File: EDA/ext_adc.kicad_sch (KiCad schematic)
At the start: 10 parts, among them U1 ADS1115IDGS, U2 ADS1115IDGS

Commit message: Renumber schematic
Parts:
- renumbered C4 to C13, C5 to C14, R1 to R42, R2 to R43, R3 to R44, R4 to R45, R5 to R46, R6 to R47, U1 to U7, U2 to U8
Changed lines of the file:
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@@
   (symbol (lib_id "Library:R") (at 114.3 124.46 0) (unit 1)
     (in_bom yes) (on_board yes) (dnp no)
-    (property "Reference" "R3" (at 113.03 119.38 90)
+    (property "Reference" "R44" (at 113.03 119.38 90)
       (effects (font (size 1.27 1.27)) hide)
     )
@@
       (project "DiveCAN Head2"
         (path "/ab021047-3849-453b-b3dc-d234ace3779d/43f35934-7d95-448c-989a-d83dd71666be"
-          (reference "R3") (unit 1)
+          (reference "R44") (unit 1)
         )
       )
@@
   (symbol (lib_id "Library:R") (at 114.3 132.08 0) (unit 1)
     (in_bom yes) (on_board yes) (dnp no)
-    (property "Reference" "R4" (at 113.03 127 90)
+    (property "Reference" "R45" (at 113.03 127 90)
       (effects (font (size 1.27 1.27)) hide)
     )
@@
       (project "DiveCAN Head2"
         (path "/ab021047-3849-453b-b3dc-d234ace3779d/43f35934-7d95-448c-989a-d83dd71666be"
-          (reference "R4") (unit 1)
+          (reference "R45") (unit 1)
         )
       )
@@
   (symbol (lib_id "Library:ADS1115IDGS") (at 133.35 128.27 0) (unit 1)
     (in_bom yes) (on_board yes) (dnp no) (fields_autoplaced)
-    (property "Reference" "U2" (at 135.5441 137.6101 0)
+    (property "Reference" "U8" (at 135.5441 137.6101 0)
       (effects (font (size 1.27 1.27)) (justify left))
     )
@@
       (project "DiveCAN Head2"
         (path "/ab021047-3849-453b-b3dc-d234ace3779d/43f35934-7d95-448c-989a-d83dd71666be"
-          (reference "U2") (unit 1)
+          (reference "U8") (unit 1)
         )
       )
@@
   (symbol (lib_id "Library:C") (at 139.7 55.88 0) (unit 1)
     (in_bom yes) (on_board yes) (dnp no) (fields_autoplaced)
-    (property "Reference" "C4" (at 142.621 54.856 0)
+    (property "Reference" "C13" (at 142.621 54.856 0)
       (effects (font (size 1.27 1.27)) (justify left))
     )
@@
       (project "DiveCAN Head2"
         (path "/ab021047-3849-453b-b3dc-d234ace3779d/43f35934-7d95-448c-989a-d83dd71666be"
-          (reference "C4") (unit 1)
+          (reference "C13") (unit 1)
         )
       )
@@
   (symbol (lib_id "power:GNDREF") (at 119.38 92.71 0) (unit 1)
     (in_bom yes) (on_board yes) (dnp no) (fields_autoplaced)
-    (property "Reference" "#PWR07" (at 119.38 99.06 0)
+    (property "Reference" "#PWR054" (at 119.38 99.06 0)
       (effects (font (size 1.27 1.27)) hide)
     )
@@
       (project "DiveCAN Head2"
         (path "/ab021047-3849-453b-b3dc-d234ace3779d/43f35934-7d95-448c-989a-d83dd71666be"
-          (reference "#PWR07") (unit 1)
+          (reference "#PWR054") (unit 1)
         )
       )
@@
   (symbol (lib_id "Library:R") (at 119.38 88.9 0) (unit 1)
     (in_bom yes) (on_board yes) (dnp no)
-    (property "Reference" "R6" (at 118.11 83.82 90)
+    (property "Reference" "R47" (at 118.11 83.82 90)
       (effects (font (size 1.27 1.27)) hide)
     )
@@
       (project "DiveCAN Head2"
         (path "/ab021047-3849-453b-b3dc-d234ace3779d/43f35934-7d95-448c-989a-d83dd71666be"
-          (reference "R6") (unit 1)
+          (reference "R47") (unit 1)
         )
       )
@@
   (symbol (lib_id "power:GNDREF") (at 109.22 82.55 0) (unit 1)
     (in_bom yes) (on_board yes) (dnp no) (fields_autoplaced)
-    (property "Reference" "#PWR03" (at 109.22 88.9 0)
+    (property "Reference" "#PWR052" (at 109.22 88.9 0)
       (effects (font (size 1.27 1.27)) hide)
     )
@@
       (project "DiveCAN Head2"
         (path "/ab021047-3849-453b-b3dc-d234ace3779d/43f35934-7d95-448c-989a-d83dd71666be"
-          (reference "#PWR03") (unit 1)
+          (reference "#PWR052") (unit 1)
         )
       )
@@
   (symbol (lib_id "power:GNDREF") (at 114.3 135.89 0) (unit 1)
     (in_bom yes) (on_board yes) (dnp no) (fields_autoplaced)
-    (property "Reference" "#PWR04" (at 114.3 142.24 0)
+    (property "Reference" "#PWR053" (at 114.3 142.24 0)
       (effects (font (size 1.27 1.27)) hide)
     )
@@
       (project "DiveCAN Head2"
         (path "/ab021047-3849-453b-b3dc-d234ace3779d/43f35934-7d95-448c-989a-d83dd71666be"
-          (reference "#PWR04") (unit 1)
+          (reference "#PWR053") (unit 1)
         )
       )
@@
   (symbol (lib_id "power:GNDREF") (at 133.35 138.43 0) (unit 1)
     (in_bom yes) (on_board yes) (dnp no) (fields_autoplaced)
-    (property "Reference" "#PWR012" (at 133.35 144.78 0)
+    (property "Reference" "#PWR056" (at 133.35 144.78 0)
       (effects (font (size 1.27 1.27)) hide)
     )
@@
       (project "DiveCAN Head2"
         (path "/ab021047-3849-453b-b3dc-d234ace3779d/43f35934-7d95-448c-989a-d83dd71666be"
-          (reference "#PWR012") (unit 1)
+          (reference "#PWR056") (unit 1)
         )
       )
@@
   (symbol (lib_id "Library:R") (at 109.22 71.12 0) (unit 1)
     (in_bom yes) (on_board yes) (dnp no)
-    (property "Reference" "R1" (at 107.95 66.04 90)
+    (property "Reference" "R42" (at 107.95 66.04 90)
       (effects (font (size 1.27 1.27)) hide)
     )
@@
       (project "DiveCAN Head2"
         (path "/ab021047-3849-453b-b3dc-d234ace3779d/43f35934-7d95-448c-989a-d83dd71666be"
-          (reference "R1") (unit 1)
+          (reference "R42") (unit 1)
         )
       )
@@
   (symbol (lib_id "Library:R") (at 119.38 81.28 0) (unit 1)
     (in_bom yes) (on_board yes) (dnp no)
-    (property "Reference" "R5" (at 118.11 76.2 90)
+    (property "Reference" "R46" (at 118.11 76.2 90)
       (effects (font (size 1.27 1.27)) hide)
     )
@@
       (project "DiveCAN Head2"
         (path "/ab021047-3849-453b-b3dc-d234ace3779d/43f35934-7d95-448c-989a-d83dd71666be"
-          (reference "R5") (unit 1)
+          (reference "R46") (unit 1)
         )
       )
@@
   (symbol (lib_id "power:GNDREF") (at 143.51 80.01 90) (unit 1)
     (in_bom yes) (on_board yes) (dnp no) (fields_autoplaced)
-    (property "Reference" "#PWR015" (at 149.86 80.01 0)
+    (property "Reference" "#PWR059" (at 149.86 80.01 0)
       (effects (font (size 1.27 1.27)) hide)
     )
@@
       (project "DiveCAN Head2"
         (path "/ab021047-3849-453b-b3dc-d234ace3779d/43f35934-7d95-448c-989a-d83dd71666be"
-          (reference "#PWR015") (unit 1)
+          (reference "#PWR059") (unit 1)
         )
       )
@@
   (symbol (lib_id "Library:R") (at 109.22 78.74 0) (unit 1)
     (in_bom yes) (on_board yes) (dnp no)
-    (property "Reference" "R2" (at 107.95 73.66 90)
+    (property "Reference" "R43" (at 107.95 73.66 90)
       (effects (font (size 1.27 1.27)) hide)
     )
@@
       (project "DiveCAN Head2"
         (path "/ab021047-3849-453b-b3dc-d234ace3779d/43f35934-7d95-448c-989a-d83dd71666be"
-          (reference "R2") (unit 1)
+          (reference "R43") (unit 1)
         )
       )
@@
   (symbol (lib_id "Library:C") (at 140.97 109.22 0) (unit 1)
     (in_bom yes) (on_board yes) (dnp no) (fields_autoplaced)
-    (property "Reference" "C5" (at 143.891 108.0079 0)
+    (property "Reference" "C14" (at 143.891 108.0079 0)
       (effects (font (size 1.27 1.27)) (justify left))
     )
@@
       (project "DiveCAN Head2"
         (path "/ab021047-3849-453b-b3dc-d234ace3779d/43f35934-7d95-448c-989a-d83dd71666be"
-          (reference "C5") (unit 1)
+          (reference "C14") (unit 1)
         )
       )
@@
   (symbol (lib_id "power:GNDREF") (at 133.35 85.09 0) (unit 1)
     (in_bom yes) (on_board yes) (dnp no) (fields_autoplaced)
-    (property "Reference" "#PWR010" (at 133.35 91.44 0)
+    (property "Reference" "#PWR055" (at 133.35 91.44 0)
       (effects (font (size 1.27 1.27)) hide)
     )
@@
       (project "DiveCAN Head2"
         (path "/ab021047-3849-453b-b3dc-d234ace3779d/43f35934-7d95-448c-989a-d83dd71666be"
-          (reference "#PWR010") (unit 1)
+          (reference "#PWR055") (unit 1)
         )
       )
@@
   (symbol (lib_id "power:GNDREF") (at 139.7 59.69 0) (unit 1)
     (in_bom yes) (on_board yes) (dnp no)
-    (property "Reference" "#PWR013" (at 139.7 66.04 0)
+    (property "Reference" "#PWR057" (at 139.7 66.04 0)
       (effects (font (size 1.27 1.27)) hide)
     )
@@
       (project "DiveCAN Head2"
         (path "/ab021047-3849-453b-b3dc-d234ace3779d/43f35934-7d95-448c-989a-d83dd71666be"
-          (reference "#PWR013") (unit 1)
+          (reference "#PWR057") (unit 1)
         )
       )
@@
   (symbol (lib_id "power:GNDREF") (at 140.97 113.03 0) (unit 1)
     (in_bom yes) (on_board yes) (dnp no)
-    (property "Reference" "#PWR014" (at 140.97 119.38 0)
+    (property "Reference" "#PWR058" (at 140.97 119.38 0)
       (effects (font (size 1.27 1.27)) hide)
     )
@@
       (project "DiveCAN Head2"
         (path "/ab021047-3849-453b-b3dc-d234ace3779d/43f35934-7d95-448c-989a-d83dd71666be"
-          (reference "#PWR014") (unit 1)
+          (reference "#PWR058") (unit 1)
         )
       )
@@
   (symbol (lib_id "Library:ADS1115IDGS") (at 133.35 74.93 0) (unit 1)
     (in_bom yes) (on_board yes) (dnp no) (fields_autoplaced)
-    (property "Reference" "U1" (at 135.5441 84.2701 0)
+    (property "Reference" "U7" (at 135.5441 84.2701 0)
       (effects (font (size 1.27 1.27)) (justify left))
     )
@@
       (project "DiveCAN Head2"
         (path "/ab021047-3849-453b-b3dc-d234ace3779d/43f35934-7d95-448c-989a-d83dd71666be"
-          (reference "U1") (unit 1)
-        )
-      )
+          (reference "U7") (unit 1)
+        )
+      )

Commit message: Move power logic into power distribution sheet
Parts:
- renumbered C13 to C15, C14 to C16, R42 to R36, R43 to R37, R44 to R38, R45 to R39, R46 to R40, R47 to R41, U7 to U5, U8 to U6

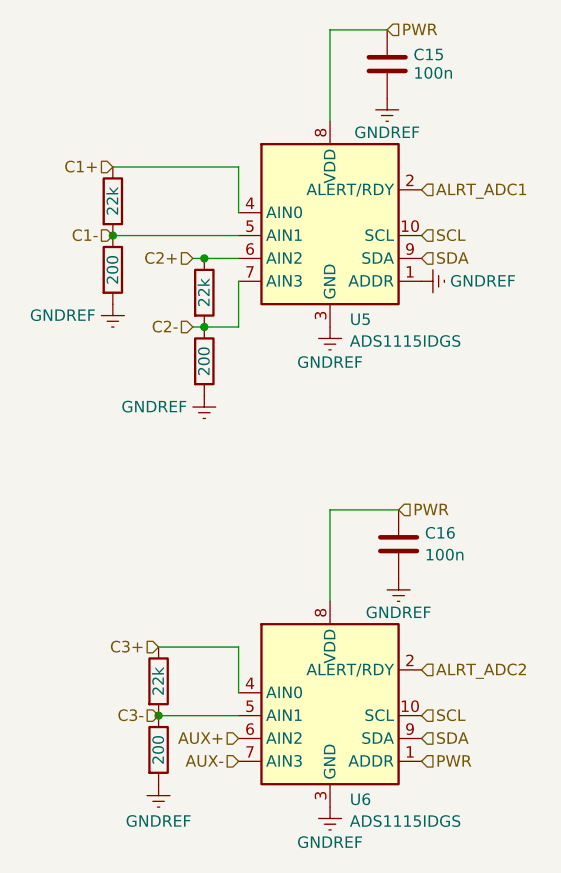
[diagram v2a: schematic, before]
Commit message: Comment schematic
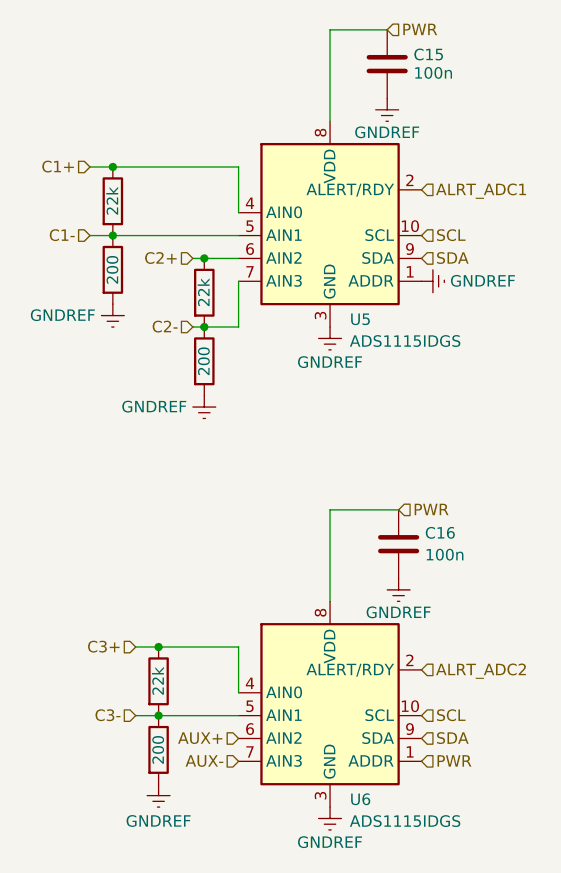
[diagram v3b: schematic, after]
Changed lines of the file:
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@@
 (kicad_sch (version 20230121) (generator eeschema)
   (paper "A4")
+  (junction (at 109.22 67.31) (diameter 0) (color 0 0 0 0)
+  )
   (junction (at 119.38 85.09) (diameter 0) (color 0 0 0 0)
   )
@@
   (junction (at 109.22 74.93) (diameter 0) (color 0 0 0 0)
   )
+  (junction (at 114.3 120.65) (diameter 0) (color 0 0 0 0)
+  )
   (wire (pts (xy 133.35 105.41) (xy 140.97 105.41))
     (stroke (width 0) (type default))
   )
   (wire (pts (xy 123.19 67.31) (xy 123.19 72.39))
+    (stroke (width 0) (type default))
+  )
+  (wire (pts (xy 111.76 120.65) (xy 114.3 120.65))
     (stroke (width 0) (type default))
   )
@@
     (stroke (width 0) (type default))
   )
+  (wire (pts (xy 106.68 74.93) (xy 109.22 74.93))
+    (stroke (width 0) (type default))
+  )
   (wire (pts (xy 123.19 85.09) (xy 123.19 80.01))
+    (stroke (width 0) (type default))
+  )
+  (wire (pts (xy 114.3 128.27) (xy 123.19 128.27))
     (stroke (width 0) (type default))
   )
@@
     (stroke (width 0) (type default))
   )
+  (wire (pts (xy 111.76 128.27) (xy 114.3 128.27))
+    (stroke (width 0) (type default))
+  )
   (wire (pts (xy 119.38 77.47) (xy 123.19 77.47))
+    (stroke (width 0) (type default))
+  )
+  (wire (pts (xy 109.22 67.31) (xy 123.19 67.31))
     (stroke (width 0) (type default))
   )
@@
     (stroke (width 0) (type default))
   )
-  (wire (pts (xy 109.22 67.31) (xy 123.19 67.31))
-    (stroke (width 0) (type default))
-  )
-  (wire (pts (xy 114.3 128.27) (xy 123.19 128.27))
+  (wire (pts (xy 106.68 67.31) (xy 109.22 67.31))
     (stroke (width 0) (type default))
   )
@@
     (effects (font (size 1.27 1.27)) (justify right))
   )
-  (hierarchical_label "C1+" (shape input) (at 109.22 67.31 180) (fields_autoplaced)
+  (hierarchical_label "C1+" (shape input) (at 106.68 67.31 180) (fields_autoplaced)
     (effects (font (size 1.27 1.27)) (justify right))
   )
-  (hierarchical_label "C3-" (shape input) (at 114.3 128.27 180) (fields_autoplaced)
+  (hierarchical_label "C3-" (shape input) (at 111.76 128.27 180) (fields_autoplaced)
     (effects (font (size 1.27 1.27)) (justify right))
   )
@@
     (effects (font (size 1.27 1.27)) (justify left))
   )
-  (hierarchical_label "C1-" (shape input) (at 109.22 74.93 180) (fields_autoplaced)
+  (hierarchical_label "C1-" (shape input) (at 106.68 74.93 180) (fields_autoplaced)
     (effects (font (size 1.27 1.27)) (justify right))
   )
@@
     (effects (font (size 1.27 1.27)) (justify right))
   )
-  (hierarchical_label "C3+" (shape input) (at 114.3 120.65 180) (fields_autoplaced)
+  (hierarchical_label "C3+" (shape input) (at 111.76 120.65 180) (fields_autoplaced)
     (effects (font (size 1.27 1.27)) (justify right))
   )
